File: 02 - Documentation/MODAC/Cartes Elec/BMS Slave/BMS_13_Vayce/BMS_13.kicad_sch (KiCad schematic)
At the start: 108 parts, among them IC1 LT3990EMSE#TRPBF, IC2 LTC6255IS6#TRMPBF, IC3 ADG728BRUZ-REEL7, IC4 ADG728BRUZ-REEL7, J1 Conn_01x02_Pin, J2 Conn_01x07_Pin, J3 Conn_01x02_Pin, J4 Conn_01x08_Pin, J5 Conn_01x08_Pin, J6 Conn_01x07_Pin, Q1 Q_PMOS_GDS, Q10 Q_PMOS_GDS, Q11 Q_PMOS_GDS, Q12 Q_PMOS_GDS, Q18 Q_PMOS_GDS, Q2 Q_PMOS_GDS, Q3 Q_PMOS_GDS, Q4 Q_PMOS_GDS, Q5 Q_PMOS_GDS, Q6 Q_PMOS_GDS, Q7 Q_PMOS_GDS, Q8 Q_PMOS_GDS, Q9 Q_PMOS_GDS, T1 SM91501ALE, U1 ADBMS1818ASWZ

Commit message: bien_relié
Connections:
- net VREF2: now also C11.2, U1.50 (VREF2)
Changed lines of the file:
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@@
 	)
 	(junction
+		(at 218.44 185.42)
+		(diameter 0)
+		(color 0 0 0 0)
+	)
+	(junction
 		(at 283.21 120.65)
 		(diameter 0)
@@
 	(wire
 		(pts
+			(xy 218.44 185.42) (xy 218.44 187.96)
+		)
+		(stroke
+			(width 0)
+			(type default)
+		)
+	)
+	(wire
+		(pts
 			(xy 283.21 262.89) (xy 284.48 262.89)
 		)
@@
 	(wire
 		(pts
+			(xy 189.23 185.42) (xy 218.44 185.42)
+		)
+		(stroke
+			(width 0)
+			(type default)
+		)
+	)
+	(wire
+		(pts
 			(xy 257.81 132.08) (xy 257.81 133.35)
 		)
@@
 	(wire
 		(pts
-			(xy 232.41 185.42) (xy 189.23 185.42)
-		)
-		(stroke
-			(width 0)
-			(type default)
-		)
-	)
-	(wire
-		(pts
 			(xy 196.85 190.5) (xy 189.23 190.5)
 		)
@@
 	(wire
 		(pts
+			(xy 218.44 185.42) (xy 232.41 185.42)
+		)
+		(stroke
+			(width 0)
+			(type default)
+		)
+	)
+	(wire
+		(pts
 			(xy 283.21 39.37) (xy 284.48 39.37)
 		)
@@
 		(fields_autoplaced yes)
 		(effects
+			(font
+				(size 1.27 1.27)
+			)
+			(justify left bottom)
+		)
+	)
+	(label "VREF2"
+		(at 218.44 187.96 0)
+		(fields_autoplaced yes)
+		(effects

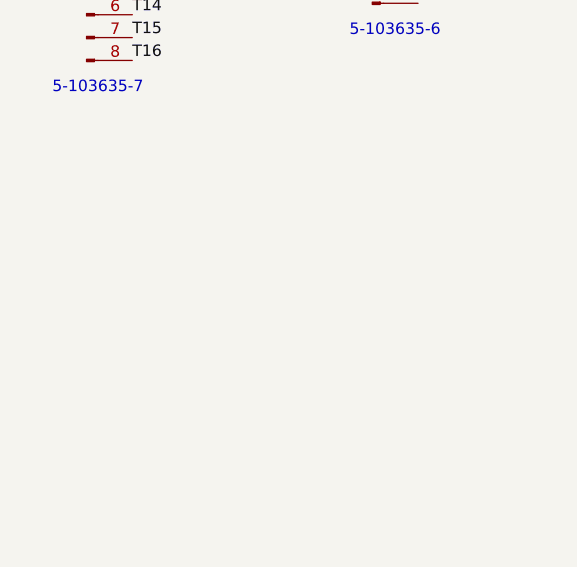
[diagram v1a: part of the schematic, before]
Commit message: Modif bms13
Déplacement et autres
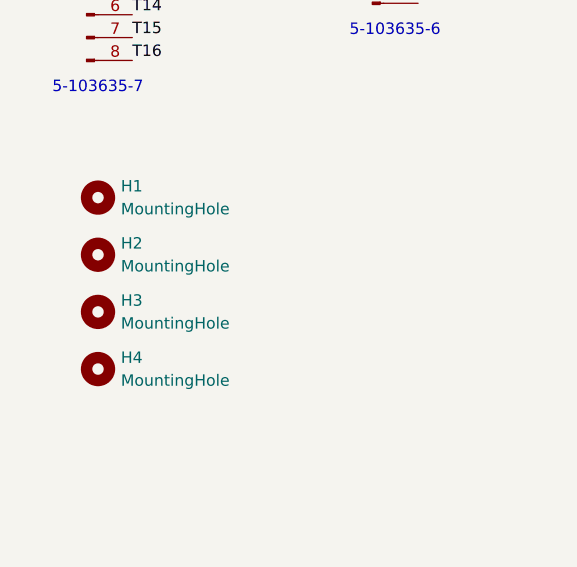
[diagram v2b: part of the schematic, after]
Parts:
- added H1, H2, H3, H4: MountingHole, MountingHole:MountingHole_3.2mm_M3_DIN965_Pad, symbol Mechanical:MountingHole

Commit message: Ajout du VDC-  aux connecteurs BMS + fichiers de prod + TS Schematic update
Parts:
- removed J4, J5: Conn_01x08_Pin, EPSA:SHDRRA9W69P0X254_1X9_2527X1359X741P, symbol Connector:Conn_01x08_Pin
- added J7, J8: Conn_01x09_Pin, 5-1049359:51049359, symbol Connector:Conn_01x09_Pin
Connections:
- net -VDC: now also J7.9 (Pin_9), J8.1 (Pin_1)
- net T1: now also J7.1 (Pin_1)
- net T10: now also J8.3 (Pin_3)
- net T11: now also J8.4 (Pin_4)
- net T12: now also J8.5 (Pin_5)
- net T13: now also J8.6 (Pin_6)
- net T14: now also J8.7 (Pin_7)
- net T15: now also J8.8 (Pin_8)
- net T16: now also J8.9 (Pin_9)
- net T2: now also J7.2 (Pin_2)
- net T3: now also J7.3 (Pin_3)
- net T4: now also J7.4 (Pin_4)
- net T5: now also J7.5 (Pin_5)
- net T6: now also J7.6 (Pin_6)
- net T7: now also J7.7 (Pin_7)
- net T8: now also J7.8 (Pin_8)
- net T9: now also J8.2 (Pin_2)
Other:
- note added: "5-104935-9"
- note removed: "5-103635-7"

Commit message: Restauration version Axel de février 2025
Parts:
- removed J7, J8: Conn_01x09_Pin, 5-1049359:51049359, symbol Connector:Conn_01x09_Pin
- added J4, J5: Conn_01x08_Pin, EPSA:SHDRRA9W69P0X254_1X9_2527X1359X741P, symbol Connector:Conn_01x08_Pin
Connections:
- net T1: now also J4.1 (Pin_1)
- net T10: now also J5.2 (Pin_2)
- net T11: now also J5.3 (Pin_3)
- net T12: now also J5.4 (Pin_4)
- net T13: now also J5.5 (Pin_5)
- net T14: now also J5.6 (Pin_6)
- net T15: now also J5.7 (Pin_7)
- net T16: now also J5.8 (Pin_8)
- net T2: now also J4.2 (Pin_2)
- net T3: now also J4.3 (Pin_3)
- net T4: now also J4.4 (Pin_4)
- net T5: now also J4.5 (Pin_5)
- net T6: now also J4.6 (Pin_6)
- net T7: now also J4.7 (Pin_7)
- net T8: now also J4.8 (Pin_8)
- net T9: now also J5.1 (Pin_1)
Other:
- note added: "5-103635-7"
- note removed: "5-104935-9"
